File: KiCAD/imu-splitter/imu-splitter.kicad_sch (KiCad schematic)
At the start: 16 parts, among them J1 4P4C, J2 4P4C, J3 4P4C, J4 4P4C, J5 4P4C, J6 4P4C, J7 3220-26-0200-00, J8 Conn_01x04, J9 Conn_01x05, U1 AZ1117-3.3

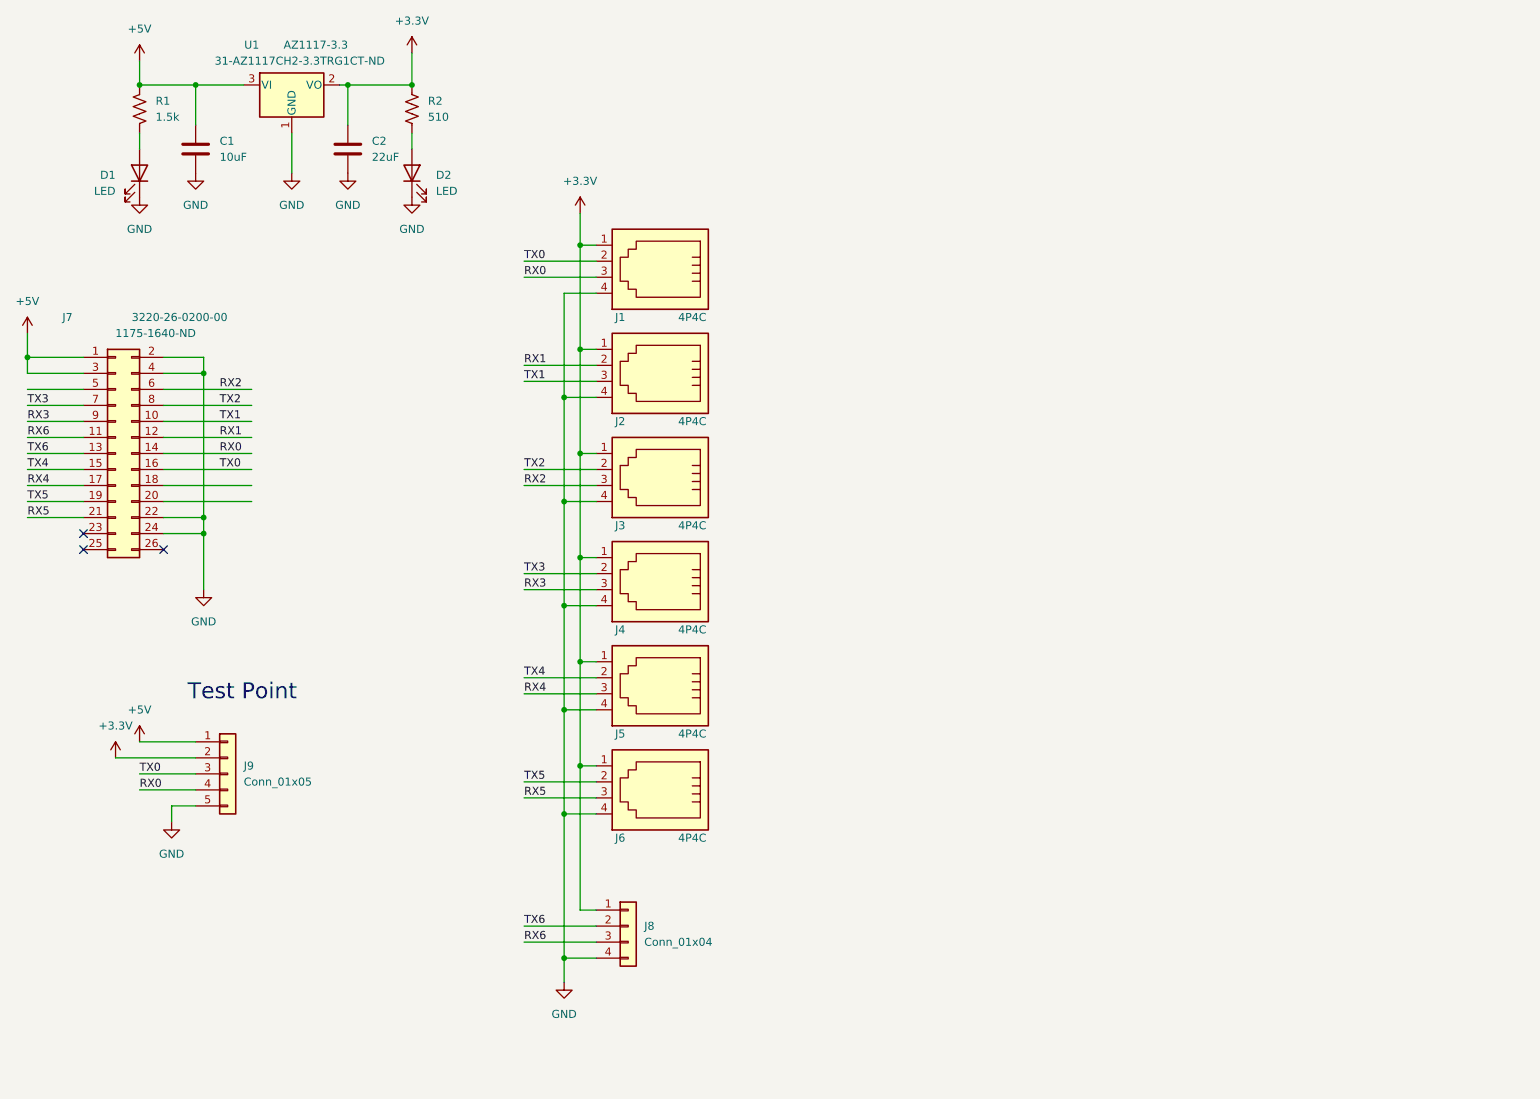
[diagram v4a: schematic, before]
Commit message: Update schematic for correct U1 part number
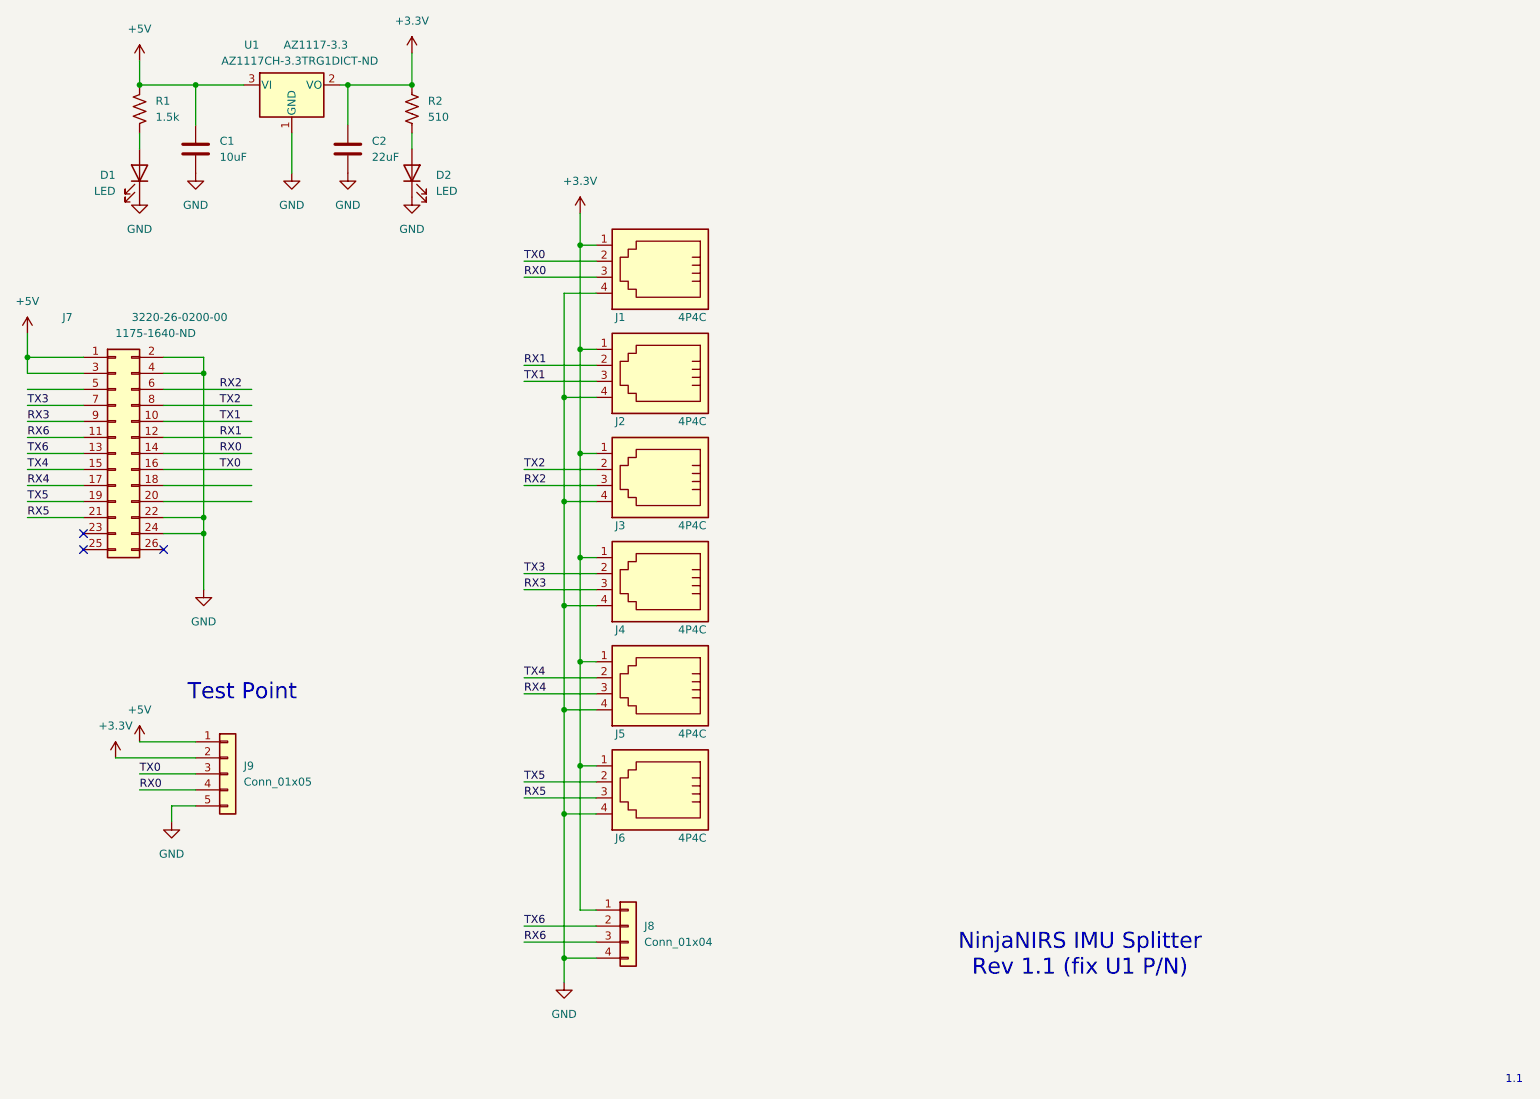
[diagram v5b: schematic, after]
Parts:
- U1: CatNo 31-AZ1117CH2-3.3TRG1CT-ND -> AZ1117CH-3.3TRG1DICT-ND; MfgNo AZ1117CH2-3.3TRG1 -> AZ1117CH-3.3TRG1
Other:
- note added: "1.1"
- note added: "NinjaNIRS IMU Splitter Rev 1.1 (fix U1 P/N)"
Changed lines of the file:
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@@
+		)
+	)
+	(text "1.1"
+		(exclude_from_sim no)
+		(at 271.272 193.294 0)
+		(effects
+			(font
+				(size 1.27 1.27)
+			)
 		)
 	)
@@
 			)
 			(justify left bottom)
+		)
+	)
+	(text "NinjaNIRS IMU Splitter\nRev 1.1 (fix U1 P/N)"
+		(exclude_from_sim no)
+		(at 202.438 173.482 0)
+		(effects
+			(font
+				(size 2.54 2.54)
+			)
 		)
 	)
@@
 			)
 		)
-		(property "CatNo" "31-AZ1117CH2-3.3TRG1CT-ND"
+		(property "CatNo" "AZ1117CH-3.3TRG1DICT-ND"
 			(at 78.74 31.75 0)
 			(effects
@@
 			)
 		)
-		(property "MfgNo" "AZ1117CH2-3.3TRG1"
+		(property "MfgNo" "AZ1117CH-3.3TRG1"
 			(at 77.47 35.56 0)
 			(effects

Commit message: Update splitter to V2.0
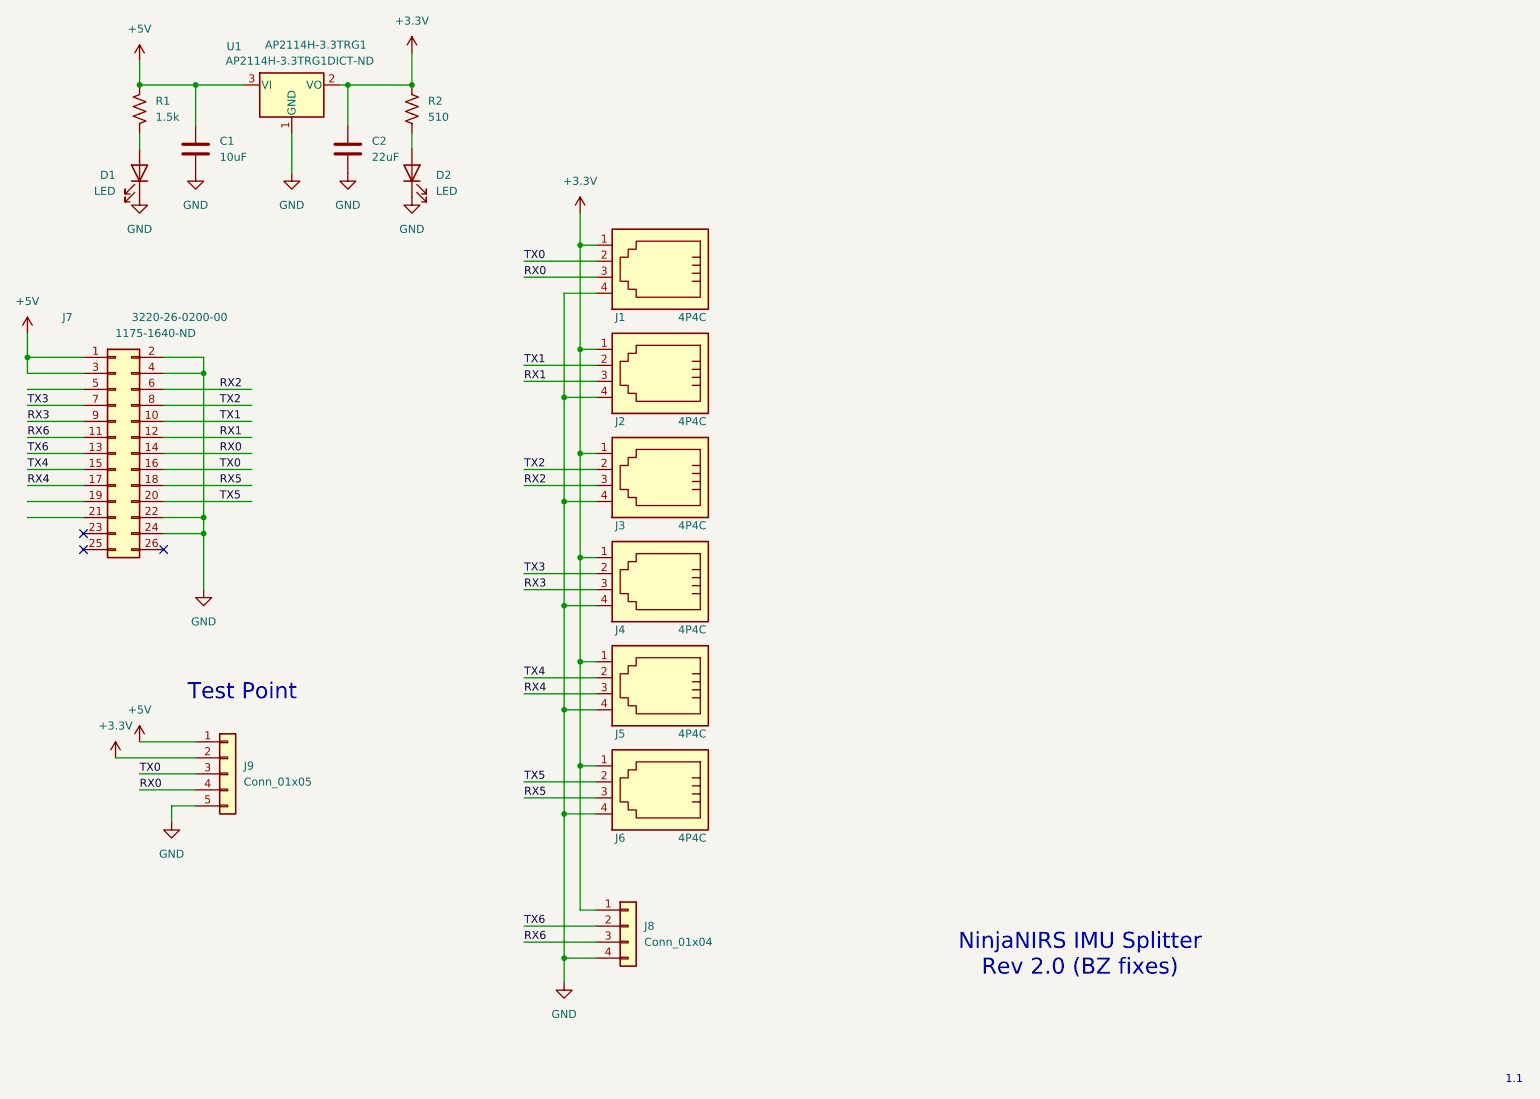
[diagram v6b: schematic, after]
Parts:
- U1: value AZ1117-3.3 -> AP2114H-3.3TRG1; CatNo AZ1117CH-3.3TRG1DICT-ND -> AP2114H-3.3TRG1DICT-ND
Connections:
- net RX1: now also J2.3; no longer J2.2
- net RX5: now also J7.18 (Pin_18); no longer J7.21 (Pin_21)
- net TX1: now also J2.2; no longer J2.3
- net TX5: now also J7.20 (Pin_20); no longer J7.19 (Pin_19)
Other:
- note added: "NinjaNIRS IMU Splitter Rev 2.0 (BZ fixes)"
- note removed: "NinjaNIRS IMU Splitter Rev 1.1 (fix U1 P/N)"
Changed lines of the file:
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@@
 		)
 	)
-	(text "NinjaNIRS IMU Splitter\nRev 1.1 (fix U1 P/N)"
+	(text "NinjaNIRS IMU Splitter\nRev 2.0 (BZ fixes)"
 		(exclude_from_sim no)
 		(at 202.438 173.482 0)
@@
 	)
 	(label "TX1"
-		(at 114.3 82.55 0)
+		(at 114.3 80.01 0)
 		(fields_autoplaced yes)
 		(effects
@@
 	)
 	(label "TX5"
-		(at 35.56 101.6 0)
+		(at 66.04 101.6 0)
 		(fields_autoplaced yes)
 		(effects
@@
 	)
 	(label "RX5"
-		(at 35.56 104.14 0)
+		(at 66.04 99.06 0)
 		(fields_autoplaced yes)
 		(effects
@@
 	)
 	(label "RX1"
-		(at 114.3 80.01 0)
+		(at 114.3 82.55 0)
 		(fields_autoplaced yes)
 		(effects
@@
 		(dnp no)
 		(property "Reference" "U1"
-			(at 71.12 29.21 0)
-			(effects
-				(font
-					(size 1.27 1.27)
-				)
-			)
-		)
-		(property "Value" "AZ1117-3.3"
+			(at 68.326 29.464 0)
+			(effects
+				(font
+					(size 1.27 1.27)
+				)
+			)
+		)
+		(property "Value" "AP2114H-3.3TRG1"
 			(at 81.28 29.21 0)
 			(effects
@@
 			)
 		)
-		(property "CatNo" "AZ1117CH-3.3TRG1DICT-ND"
+		(property "CatNo" "AP2114H-3.3TRG1DICT-ND"
 			(at 78.74 31.75 0)
 			(effects

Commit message: working on 3D of box
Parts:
- added N1: 1551T, models:1551T, symbol Mechanical:Housing
- added N2: 1551T_lid, models:1551T_lid, symbol Mechanical:Housing
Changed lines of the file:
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@@
+	)
+	(symbol
+		(lib_id "Mechanical:Housing")
+		(at 45.72 175.26 0)
+		(unit 1)
+		(exclude_from_sim yes)
+		(in_bom yes)
+		(on_board yes)
+		(dnp no)
+		(fields_autoplaced yes)
+		(property "Reference" "N1"
+			(at 49.53 174.3074 0)
+			(effects
+				(font
+					(size 1.27 1.27)
+				)
+				(justify left)
+			)
+		)
+		(property "Value" "1551T"
+			(at 49.53 176.8474 0)
+			(effects
+				(font
+					(size 1.27 1.27)
+				)
+				(justify left)
+			)
+		)
+		(property "Footprint" "models:1551T"
+			(at 46.99 173.99 0)
+			(effects
+				(font
+					(size 1.27 1.27)
+				)
+				(hide yes)
+			)
+		)
+		(property "Datasheet" "~"
+			(at 46.99 173.99 0)
+			(effects
+				(font
+					(size 1.27 1.27)
+				)
+				(hide yes)
+			)
+		)
+		(property "Description" "Housing"
+			(at 45.72 175.26 0)
+			(effects
+				(font
+					(size 1.27 1.27)
+				)
+				(hide yes)
+			)
+		)
+		(instances
+			(project "imu-splitter"
+				(path "/3ddff065-8308-49ba-816e-3ac23a1c142d"
+					(reference "N1")
+					(unit 1)
+				)
+			)
+		)
 	)
 	(symbol
@@
 					(unit 1)
 				)
+			)
+		)
+	)
+	(symbol
+		(lib_id "Mechanical:Housing")
+		(at 45.72 187.96 0)
+		(unit 1)
+		(exclude_from_sim yes)
+		(in_bom no)
+		(on_board yes)
+		(dnp yes)
+		(fields_autoplaced yes)
+		(property "Reference" "N2"
+			(at 49.53 187.0074 0)
+			(effects
+				(font
+					(size 1.27 1.27)
+				)
+				(justify left)
+			)
+		)
+		(property "Value" "1551T_lid"
+			(at 49.53 189.5474 0)
+			(effects
+				(font
+					(size 1.27 1.27)
+				)
+				(justify left)
+			)
+		)
+		(property "Footprint" "models:1551T_lid"
+			(at 46.99 186.69 0)
+			(effects
+				(font
+					(size 1.27 1.27)
+				)
+				(hide yes)
+			)
+		)
+		(property "Datasheet" "~"
+			(at 46.99 186.69 0)
+			(effects
+				(font
+					(size 1.27 1.27)
+				)
+				(hide yes)
+			)
+		)
+		(property "Description" "Housing"
+			(at 45.72 187.96 0)
+			(effects
+				(font
+					(size 1.27 1.27)
+				)
+				(hide yes)
+			)
+		)
+		(instances
+			(project "imu-splitter"
+				(path "/3ddff065-8308-49ba-816e-3ac23a1c142d"
+					(reference "N2")
+					(unit 1)
+				)

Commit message: Candidate V2 layout
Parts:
- N2: footprint models:1551T_lid -> models:1551T_lid_trans
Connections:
- net RX6: now also J7.13 (Pin_13); no longer J7.11 (Pin_11)
- net TX6: now also J7.11 (Pin_11); no longer J7.13 (Pin_13)
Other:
- note added: "2.0"
- note removed: "1.1"
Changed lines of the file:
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@@
 		)
 	)
-	(text "1.1"
+	(text "2.0"
 		(exclude_from_sim no)
 		(at 271.272 193.294 0)
@@
 	)
 	(label "RX6"
-		(at 35.56 91.44 0)
+		(at 35.56 93.98 0)
 		(fields_autoplaced yes)
 		(effects
@@
 	)
 	(label "TX6"
-		(at 35.56 93.98 0)
+		(at 35.56 91.44 0)
 		(fields_autoplaced yes)
 		(effects
@@
 		(exclude_from_sim yes)
 		(in_bom yes)
-		(on_board yes)
+		(on_board no)
 		(dnp no)
 		(fields_autoplaced yes)
@@
 		(exclude_from_sim yes)
 		(in_bom no)
-		(on_board yes)
+		(on_board no)
 		(dnp yes)
 		(fields_autoplaced yes)
@@
 			)
 		)
-		(property "Footprint" "models:1551T_lid"
+		(property "Footprint" "models:1551T_lid_trans"
 			(at 46.99 186.69 0)
 			(effects
